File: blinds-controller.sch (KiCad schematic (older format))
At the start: 15 parts, among them J1 Jack-DC, J2 Conn_01x05_Female, U1 MP1584EN-LF-Z, U2 ESP32-S2-WROOM, U3 ULN2003A

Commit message: Added MPM3610AGQV-P as a buck converter
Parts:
- removed C3: 220pF, Capacitor_SMD:C_1206_3216Metric, symbol Device:C
- removed C4: 100nF, Capacitor_SMD:C_1206_3216Metric, symbol Device:C
- removed D1: B340A-13-F, B340A-13-F:DIOM5226X240N, symbol B340A-13-F:B340A-13-F
- removed L1: SLF10145T-100M2R5-PF, SLF10145T-100:SLF10145T-100M2R5-PF, symbol SLF10145T-100:SLF10145T-100M2R5-PF
- removed R4: 200k, Resistor_SMD:R_1206_3216Metric, symbol Device:R
- removed U1: MP1584EN-LF-Z, MP1584EN-LF-Z:SOIC127P600X170-9N, symbol MP1584EN-LF-Z:MP1584EN-LF-Z
- added U1: MPM3610AGQV-P, CONV_MPM3620AGQV-P, symbol MPM3610AGQV-P:MPM3610AGQV-P
- C1: value 10uF 50V -> 10uf
- R1: value 124k -> 75k
- R2: value 40.2k -> 24k
- R3: value 68.1k -> 100k
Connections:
- net labels added: +3V3
- wire segments 49 -> 40
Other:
- note added: "Buck Converter"

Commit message: First routed version of PCB
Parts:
- U1: footprint CONV_MPM3620AGQV-P -> footprints:CONV_MPM3620AGQV-P
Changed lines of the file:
@@
 NoConn ~ 3700 7100
 $Comp
-L power:+3V3 #PWR?
+L power:+3V3 #PWR0109
 U 1 1 604567E2
 P 3250 6200
-F 0 "#PWR?" H 3250 6050 50  0001 C CNN
+F 0 "#PWR0109" H 3250 6050 50  0001 C CNN
 F 1 "+3V3" H 3265 6373 50  0000 C CNN
 F 2 "" H 3250 6200 50  0001 C CNN
@@
 $EndComp
 $Comp
-L power:+12V #PWR?
+L power:+12V #PWR0110
 U 1 1 60463AD3
 P 1600 6200
-F 0 "#PWR?" H 1600 6050 50  0001 C CNN
+F 0 "#PWR0110" H 1600 6050 50  0001 C CNN
 F 1 "+12V" H 1615 6373 50  0000 C CNN
 F 2 "" H 1600 6200 50  0001 C CNN
@@
 	3000 6200 3250 6200
 $Comp
-L power:+12V #PWR?
+L power:+12V #PWR0111
 U 1 1 60477F09
 P 1300 6050
-F 0 "#PWR?" H 1300 5900 50  0001 C CNN
+F 0 "#PWR0111" H 1300 5900 50  0001 C CNN
 F 1 "+12V" H 1315 6223 50  0000 C CNN
 F 2 "" H 1300 6050 50  0001 C CNN
@@
 	1300 6400 1800 6400
 $Comp
-L power:GND #PWR?
+L power:GND #PWR0112
 U 1 1 60487056
 P 1450 7350
-F 0 "#PWR?" H 1450 7100 50  0001 C CNN
+F 0 "#PWR0112" H 1450 7100 50  0001 C CNN
 F 1 "GND" H 1455 7177 50  0000 C CNN
 F 2 "" H 1450 7350 50  0001 C CNN
@@
 $EndComp
 $Comp
-L power:+3V3 #PWR?
+L power:+3V3 #PWR0113
 U 1 1 60488DAE
 P 1450 6650
-F 0 "#PWR?" H 1450 6500 50  0001 C CNN
+F 0 "#PWR0113" H 1450 6500 50  0001 C CNN
 F 1 "+3V3" H 1465 6823 50  0000 C CNN
 F 2 "" H 1450 6650 50  0001 C CNN
@@
 	1450 7000 1450 7050
 $Comp
-L power:+12V #PWR?
+L power:+12V #PWR0114
 U 1 1 604955B9
 P 850 6450
-F 0 "#PWR?" H 850 6300 50  0001 C CNN
+F 0 "#PWR0114" H 850 6300 50  0001 C CNN
 F 1 "+12V" H 865 6623 50  0000 C CNN
 F 2 "" H 850 6450 50  0001 C CNN
@@
 $EndComp
 $Comp
-L power:GND #PWR?
+L power:GND #PWR0115
 U 1 1 6049D114
 P 850 6750
-F 0 "#PWR?" H 850 6500 50  0001 C CNN
+F 0 "#PWR0115" H 850 6500 50  0001 C CNN
 F 1 "GND" H 855 6577 50  0000 C CNN
 F 2 "" H 850 6750 50  0001 C CNN
@@
 $EndComp
 $Comp
-L power:GND #PWR?
+L power:GND #PWR0116
 U 1 1 604A022A
 P 3600 6700
-F 0 "#PWR?" H 3600 6450 50  0001 C CNN
+F 0 "#PWR0116" H 3600 6450 50  0001 C CNN
 F 1 "GND" H 3605 6527 50  0000 C CNN
 F 2 "" H 3600 6700 50  0001 C CNN
@@
 $EndComp
 $Comp
-L power:+3V3 #PWR?
+L power:+3V3 #PWR0117
 U 1 1 604AB52D
 P 3600 6400
-F 0 "#PWR?" H 3600 6250 50  0001 C CNN
+F 0 "#PWR0117" H 3600 6250 50  0001 C CNN
 F 1 "+3V3" H 3615 6573 50  0000 C CNN
 F 2 "" H 3600 6400 50  0001 C CNN
@@
 F 0 "U1" H 2400 7270 50  0000 C CNN
 F 1 "MPM3610AGQV-P" H 2400 7179 50  0000 C CNN
-F 2 "CONV_MPM3620AGQV-P" H 2400 6500 50  0001 L BNN
+F 2 "footprints:CONV_MPM3620AGQV-P" H 2400 6500 50  0001 L BNN
 F 3 "" H 2400 6500 50  0001 L BNN
 F 4 "MPM3610AGQV-P" H 2400 6500 50  0001 L BNN "MP"
@@
 	3150 6900 3000 6900
 $Comp
-L power:GND #PWR?
+L power:GND #PWR0118
 U 1 1 604AD453
 P 3150 7200
-F 0 "#PWR?" H 3150 6950 50  0001 C CNN
+F 0 "#PWR0118" H 3150 6950 50  0001 C CNN
 F 1 "GND" H 3155 7027 50  0000 C CNN
 F 2 "" H 3150 7200 50  0001 C CNN

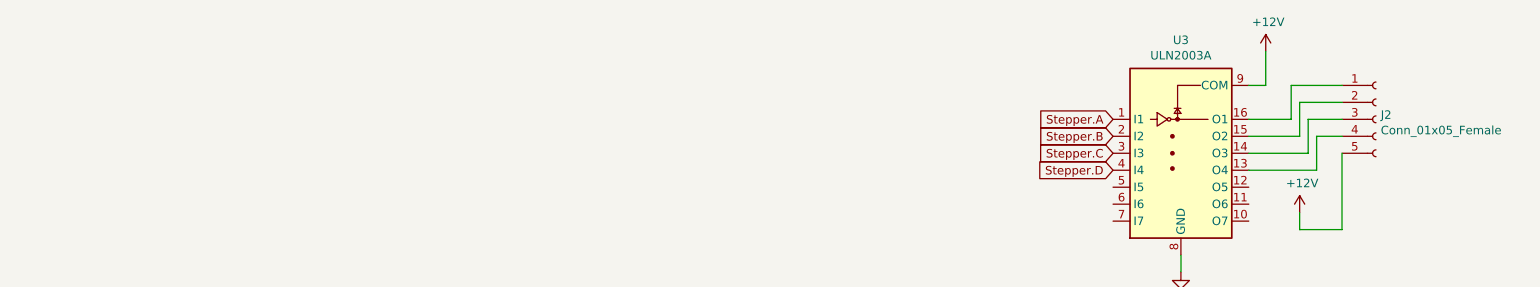
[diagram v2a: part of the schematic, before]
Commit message: Added headers for testing voltage
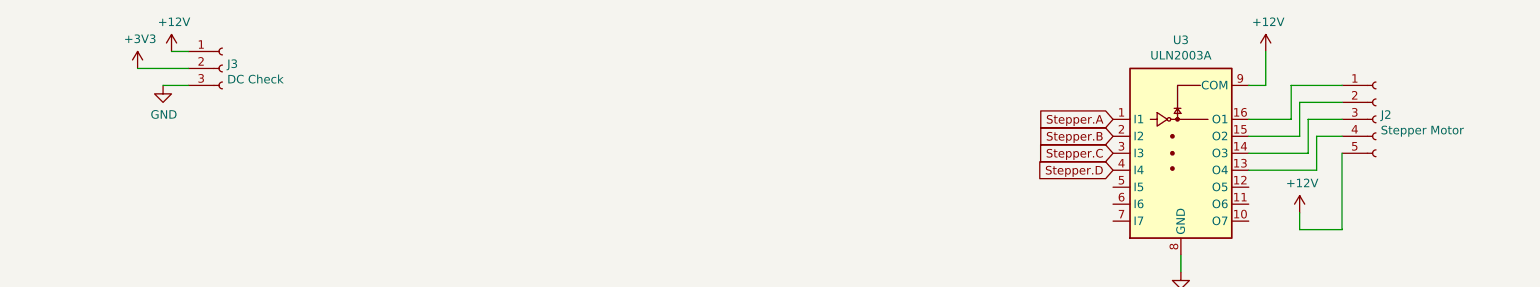
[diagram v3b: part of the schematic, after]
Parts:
- added J3: DC Check, Connector_PinHeader_2.54mm:PinHeader_1x03_P2.54mm_Vertical, symbol Connector:Conn_01x03_Female
- J2: value Conn_01x05_Female -> Stepper Motor
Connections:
- net +12V: now also J3.1 (Pin_1)
- net +3V3: now also J3.2 (Pin_2)
- net GND: now also J3.3 (Pin_3)
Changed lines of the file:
@@
 P 10350 1250
 F 0 "J2" H 10378 1276 50  0000 L CNN
-F 1 "Conn_01x05_Female" H 10378 1185 50  0000 L CNN
+F 1 "Stepper Motor" H 10378 1185 50  0000 L CNN
 F 2 "Connector_JST:JST_XH_B5B-XH-A_1x05_P2.50mm_Vertical" H 10350 1250 50  0001 C CNN
 F 3 "~" H 10350 1250 50  0001 C CNN
@@
 Text Notes 500  5400 0    50   ~ 0
 Buck Converter
+$Comp
+L Connector:Conn_01x03_Female J3
+U 1 1 6051FB9B
+P 3550 950
+F 0 "J3" H 3578 976 50  0000 L CNN
+F 1 "DC Check" H 3578 885 50  0000 L CNN
+F 2 "Connector_PinHeader_2.54mm:PinHeader_1x03_P2.54mm_Vertical" H 3550 950 50  0001 C CNN
+F 3 "~" H 3550 950 50  0001 C CNN
+	1    3550 950
+	1    0    0    -1
+$EndComp
+$Comp
+L power:GND #PWR0119
+U 1 1 60521D56
+P 3200 1050
+F 0 "#PWR0119" H 3200 800 50  0001 C CNN
+F 1 "GND" H 3205 877 50  0000 C CNN
+F 2 "" H 3200 1050 50  0001 C CNN
+F 3 "" H 3200 1050 50  0001 C CNN
+	1    3200 1050
+	1    0    0    -1
+$EndComp
+$Comp
+L power:+3V3 #PWR0120
+U 1 1 60523AE9
+P 3050 950
+F 0 "#PWR0120" H 3050 800 50  0001 C CNN
+F 1 "+3V3" H 3065 1123 50  0000 C CNN
+F 2 "" H 3050 950 50  0001 C CNN
+F 3 "" H 3050 950 50  0001 C CNN
+	1    3050 950
+	1    0    0    -1
+$EndComp
+$Comp
+L power:+12V #PWR0121
+U 1 1 605268C8
+P 3250 850
+F 0 "#PWR0121" H 3250 700 50  0001 C CNN
+F 1 "+12V" H 3265 1023 50  0000 C CNN
+F 2 "" H 3250 850 50  0001 C CNN
+F 3 "" H 3250 850 50  0001 C CNN
+	1    3250 850
+	1    0    0    -1
+$EndComp
+Wire Wire Line
+	3250 850  3350 850
+Wire Wire Line
+	3350 950  3050 950
+Wire Wire Line
+	3350 1050 3200 1050
 $EndSCHEMATC

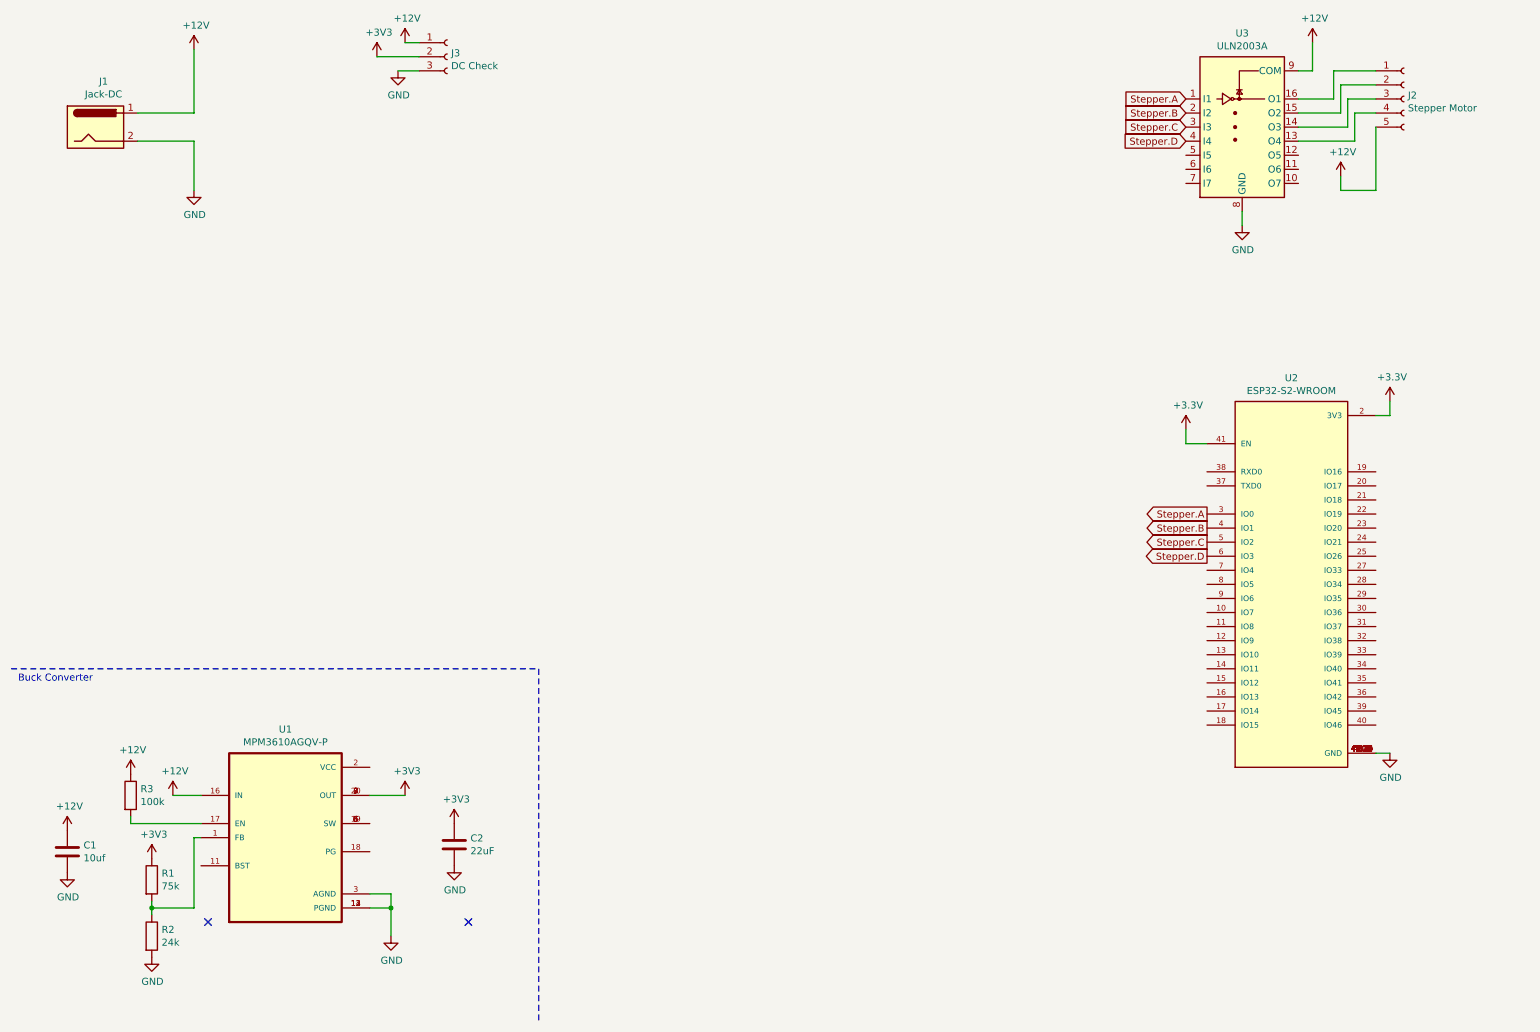
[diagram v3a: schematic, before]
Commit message: Added JTAG connector
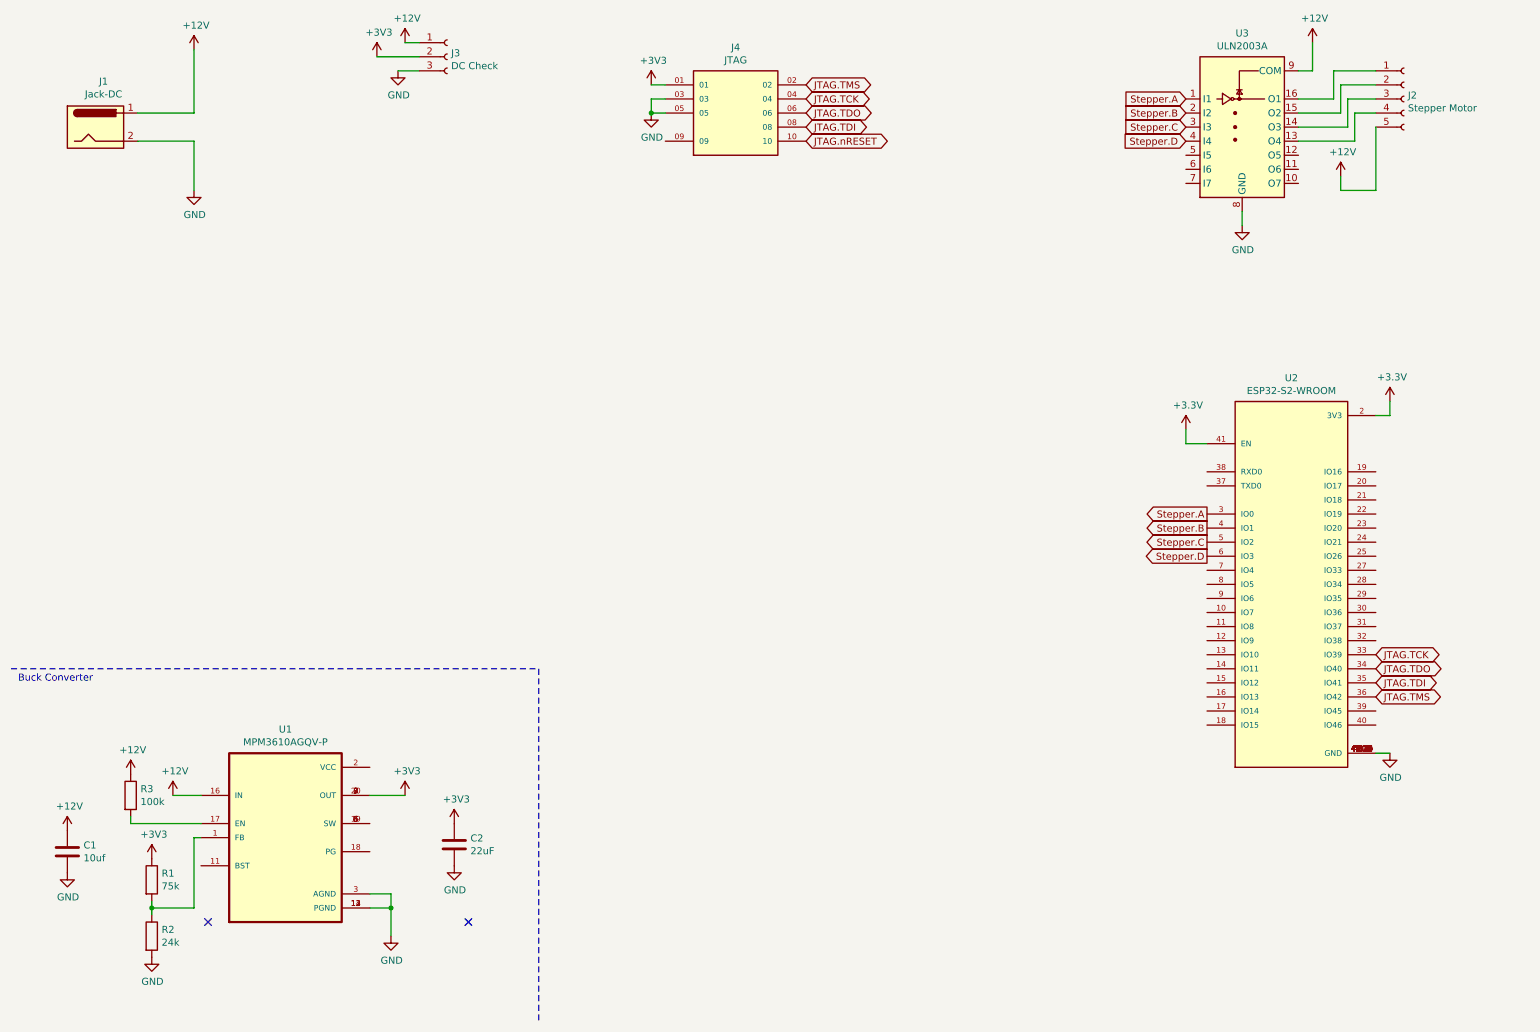
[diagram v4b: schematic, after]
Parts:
- added J4: JTAG, footprints:SAMTEC_FTSH-105-01-L-DV-007-K-P-TR, symbol FTSH-105-01-L-DV-007-K-P-TR:FTSH-105-01-L-DV-007-K-P-TR
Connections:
- net +3V3: now also J4.01
- net GND: now also J4.03, J4.05
- net JTAG.TCK: now reaches U2.33 (IO39)
- net JTAG.TCK: now also J4.04
- net JTAG.TDO: now reaches U2.34 (IO40)
- net JTAG.TDO: now also J4.06
- net JTAG.TDI: now reaches U2.35 (IO41)
- net JTAG.TDI: now also J4.08
- net JTAG.TMS: now reaches U2.36 (IO42)
- net JTAG.TMS: now also J4.02
- new net JTAG.nRESET: J4.10
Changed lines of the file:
@@
 Wire Wire Line
 	3350 1050 3200 1050
+Text GLabel 6100 1250 2    50   BiDi ~ 0
+JTAG.TCK
+Text GLabel 6100 1150 2    50   BiDi ~ 0
+JTAG.TMS
+Text GLabel 6100 1350 2    50   BiDi ~ 0
+JTAG.TDO
+Text GLabel 6100 1450 2    50   BiDi ~ 0
+JTAG.TDI
+Text GLabel 10150 5300 2    50   BiDi ~ 0
+JTAG.TDO
+Text GLabel 10150 5200 2    50   BiDi ~ 0
+JTAG.TCK
+Text GLabel 10150 5500 2    50   BiDi ~ 0
+JTAG.TMS
+Text GLabel 10150 5400 2    50   BiDi ~ 0
+JTAG.TDI
+$Comp
+L FTSH-105-01-L-DV-007-K-P-TR:FTSH-105-01-L-DV-007-K-P-TR J4
+U 1 1 605776F2
+P 5600 1350
+F 0 "J4" H 5600 1817 50  0000 C CNN
+F 1 "JTAG" H 5600 1726 50  0000 C CNN
+F 2 "footprints:SAMTEC_FTSH-105-01-L-DV-007-K-P-TR" H 5600 1350 50  0001 L BNN
+F 3 "" H 5600 1350 50  0001 L BNN
+F 4 "Samtec" H 5600 1350 50  0001 L BNN "MANUFACTURER"
+F 5 "H" H 5600 1350 50  0001 L BNN "PARTREV"
+F 6 "7.15 mm" H 5600 1350 50  0001 L BNN "MAXIMUM_PACKAGE_HEIGHT"
+F 7 "Manufacturer Recommendations" H 5600 1350 50  0001 L BNN "STANDARD"
+	1    5600 1350
+	1    0    0    -1
+$EndComp
+$Comp
+L power:+3V3 #PWR0122
+U 1 1 6057EFF5
+P 5000 1150
+F 0 "#PWR0122" H 5000 1000 50  0001 C CNN
+F 1 "+3V3" H 5015 1323 50  0000 C CNN
+F 2 "" H 5000 1150 50  0001 C CNN
+F 3 "" H 5000 1150 50  0001 C CNN
+	1    5000 1150
+	1    0    0    -1
+$EndComp
+Wire Wire Line
+	5000 1150 5100 1150
+$Comp
+L power:GND #PWR0123
+U 1 1 605809EF
+P 5000 1350
+F 0 "#PWR0123" H 5000 1100 50  0001 C CNN
+F 1 "GND" H 5005 1177 50  0000 C CNN
+F 2 "" H 5000 1350 50  0001 C CNN
+F 3 "" H 5000 1350 50  0001 C CNN
+	1    5000 1350
+	1    0    0    -1
+$EndComp
+Wire Wire Line
+	5000 1350 5100 1350
+Wire Wire Line
+	5000 1250 5000 1350
+Connection ~ 5000 1350
+Wire Wire Line
+	5000 1250 5100 1250
+Text GLabel 6100 1550 2    50   BiDi ~ 0
+JTAG.nRESET
 $EndSCHEMATC
